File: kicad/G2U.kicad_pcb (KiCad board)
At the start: 2 copper layers, 63.5 x 55.9 mm, 36 parts, among them J1 Conn_02x12_Counter_Clockwise_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

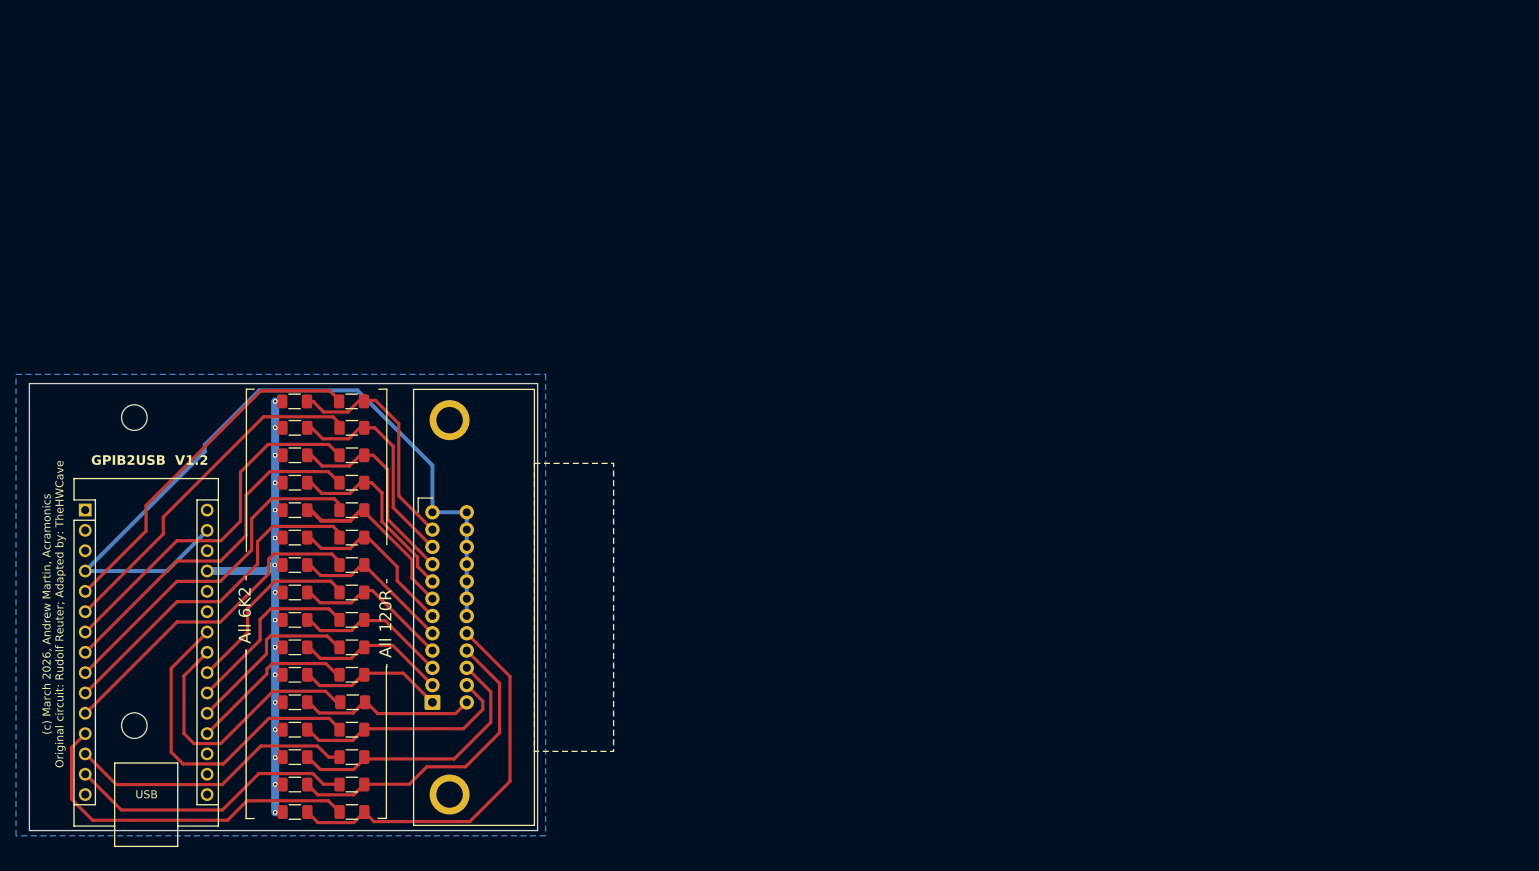
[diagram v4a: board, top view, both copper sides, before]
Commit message: Updated SMD to use a vertical Centronics connector on the back of the board and designed to fit a  83x54x30mm ABS plastic box
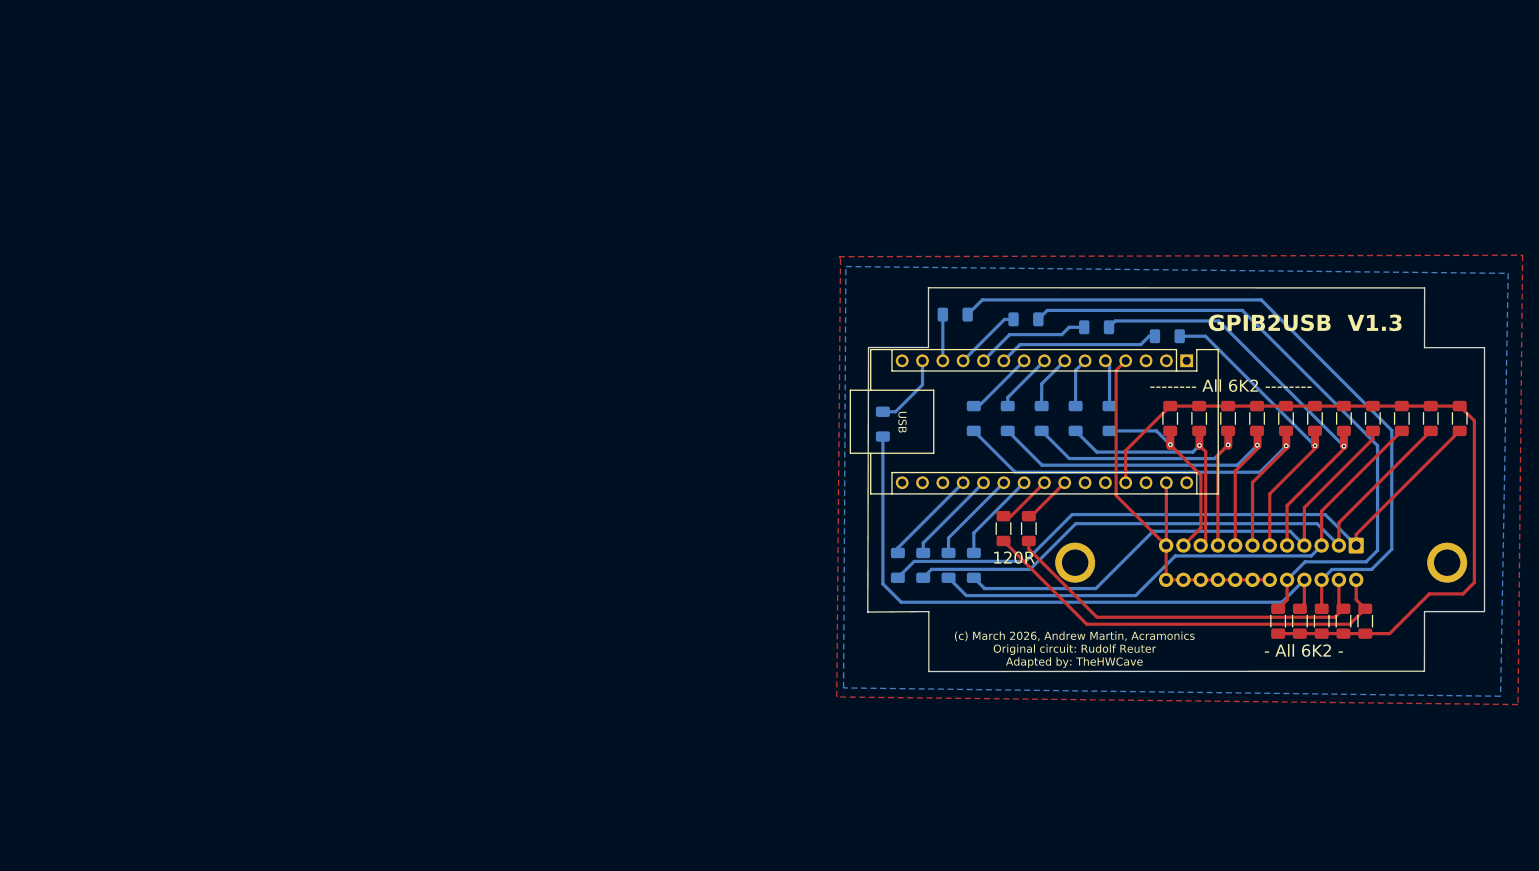
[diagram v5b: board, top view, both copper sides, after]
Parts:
- removed REF** (x2): MountingHole_3.2mm_M3, MountingHole:MountingHole_3.2mm_M3
- J1: footprint ACRM:Connector_CentronicsMale-2x12_P2.16mm_P4.29_Horizontal -> ACRM:Connector_CentronicsMale-2x12_P2.16mm_P4.29_Vertical; moved to B.Cu
- R17, R18, R19, R20, R23, R24, R25, R26, R27, R28, R29, R30, R31, R32: moved to B.Cu
- moved R1 149.1 mm to (243.3, 78.8), turned to -90 degrees
- moved R2 144.8 mm to (239.7, 78.8), turned to -90 degrees
- moved R3 140.6 mm to (236.0, 78.8), turned to -90 degrees
- moved A1 138.9 mm to (209.1, 71.6), turned to -90 degrees
- moved R4 136.5 mm to (232.4, 78.8), turned to -90 degrees
- moved R5 134.2 mm to (231.5, 104.2), turned to 90 degrees
- moved R13 132.4 mm to (228.8, 78.8), turned to -90 degrees
- moved R6 131.8 mm to (228.7, 104.2), turned to 90 degrees
- moved R15 129.5 mm to (226.0, 104.2), turned to 90 degrees
- moved R12 128.4 mm to (225.2, 78.8), turned to -90 degrees
- moved R16 127.3 mm to (223.3, 104.2), turned to 90 degrees
- moved R14 125.2 mm to (220.6, 104.2), turned to 90 degrees
- moved R11 124.4 mm to (221.6, 78.8), turned to -90 degrees
- moved R10 120.5 mm to (217.9, 78.8), turned to -90 degrees
- moved R9 116.7 mm to (214.3, 78.8), turned to -90 degrees
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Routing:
- net Net-(J1-Pin_1): track 18.4 -> 81.9 mm
- net Net-(J1-Pin_2): track 19.0 -> 75.0 mm
- net Net-(J1-Pin_15): track 34.1 -> 89.4 mm
- net Net-(J1-Pin_3): track 19.6 -> 68.6 mm
- net GND: track 97.6 -> 51.3 mm
- net Net-(J1-Pin_4): track 20.1 -> 63.5 mm
- net Net-(A1-D4): track 45.6 -> 6.86 mm
- net Net-(A1-D2): track 44.5 -> 5.88 mm
- net Net-(J1-Pin_16): track 39.8 -> 77.1 mm
- net Net-(A1-D3): track 43.4 -> 6.15 mm
- net Net-(A1-D5): track 44.6 -> 7.56 mm
- net Net-(A1-D9): track 45.1 -> 8.44 mm
- net Net-(J1-Pin_7): track 23.0 -> 58.7 mm, vias 0 -> 1
- net Net-(A1-A5): track 41.4 -> 6.22 mm
- net Net-(A1-D6): track 43.3 -> 8.63 mm
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- added copper zone on F.Cu, net GND
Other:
- board size 63.5 x 55.9 mm -> 77.1 x 48 mm
- board text added: "(c) March 2026, Andrew Martin, Acramonics Original circuit: Rudolf Reuter Adapted by: TheHWCave"
- board text added: "-- All 120R --"
- board text added: "---- All 120R ----"
- board text added: "-------- All 6K2 --------"
- board text added: "-All 120R-"
- board text added: "120R"
- board text added: "GPIB2USB V1.3"
- board text removed: "(c) March 2026, Andrew Martin, Acramonics Original circuit: Rudolf Reuter; Adapted by: TheHWCave"
- board text removed: "- All 120R -"
- board text removed: "GPIB2USB V1.2"
